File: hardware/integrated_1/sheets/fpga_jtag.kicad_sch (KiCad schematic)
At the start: 1 part, among them U1 XC6SLX9-TQG144

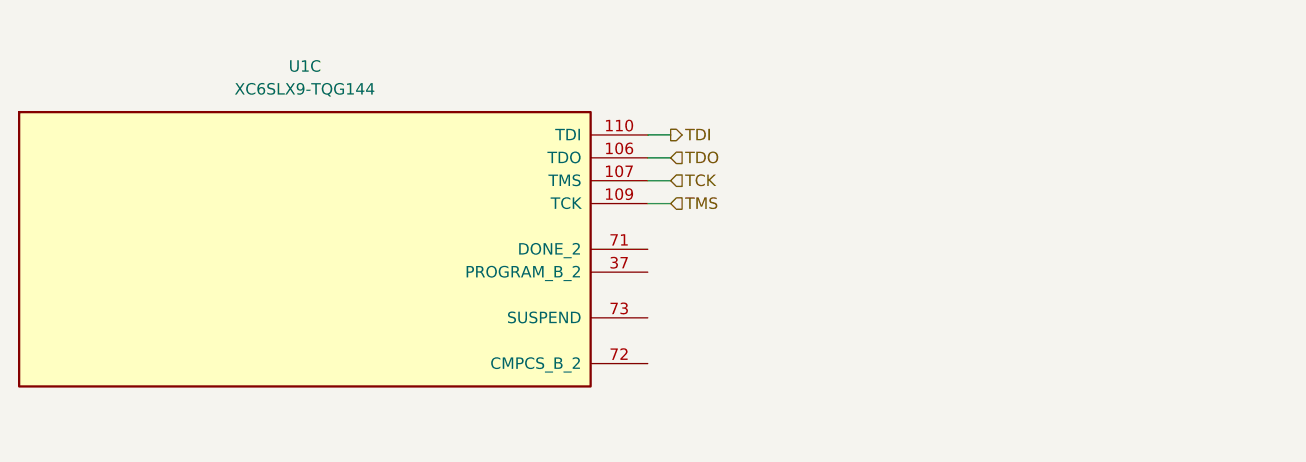
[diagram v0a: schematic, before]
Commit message: added async reset
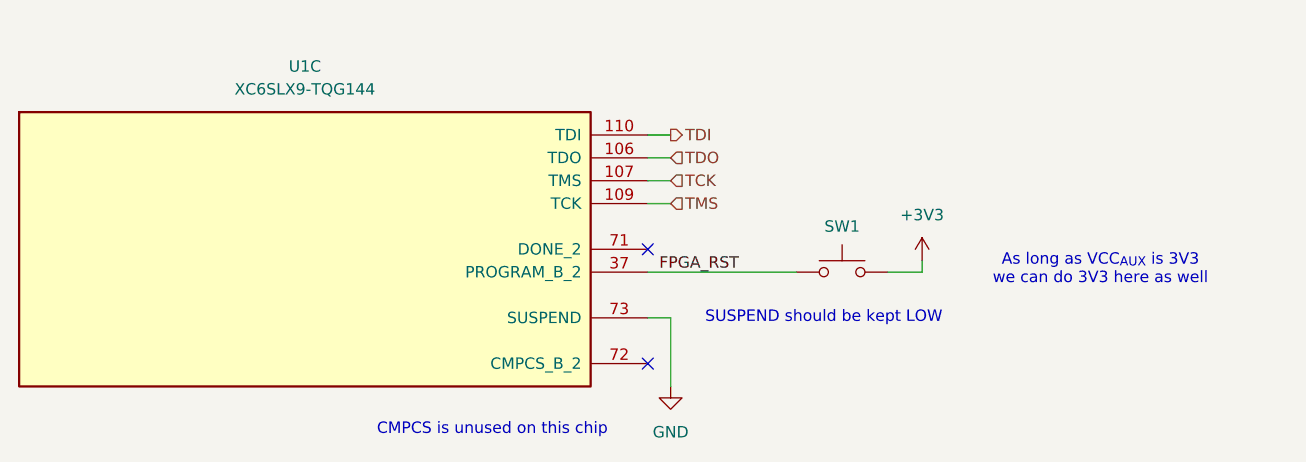
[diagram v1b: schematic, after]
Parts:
- added SW1: DNF, KiCAD Library:PTS636 SM25J SMTR LFS, symbol Switch:SW_Push
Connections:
- net FPGA_RST: now reaches U1.37 (PROGRAM_B_2)
- net FPGA_RST: now also SW1.1
- net GND: now reaches U1.73 (SUSPEND)
- new net +3V3: SW1.2
- no-connect marks 0 -> 2
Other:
- note added: "As long as VCC_{AUX} is 3V3 we can do 3V3 here as well"
- note added: "CMPCS is unused on this chip"
- note added: "SUSPEND should be kept LOW"

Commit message: finalizing the schematic and layout
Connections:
- net DONE: now reaches U1.71 (DONE_2)
- no-connect marks 2 -> 1
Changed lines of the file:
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@@
-	)
-	(no_connect
-		(at 173.99 87.63)
 	)
 	(no_connect
@@
 		)
 	)
+	(wire
+		(pts
+			(xy 176.53 87.63) (xy 173.99 87.63)
+		)
+		(stroke
+			(width 0)
+			(type default)
+		)
+	)
 	(text "SUSPEND should be kept LOW"
 		(exclude_from_sim no)
@@
 		(fields_autoplaced yes)
 		(effects
+			(font
+				(size 1.27 1.27)
+			)
+			(justify left)
+		)
+	)
+	(hierarchical_label "DONE"
+		(shape output)
+		(at 176.53 87.63 0)
+		(fields_autoplaced yes)
+		(effects

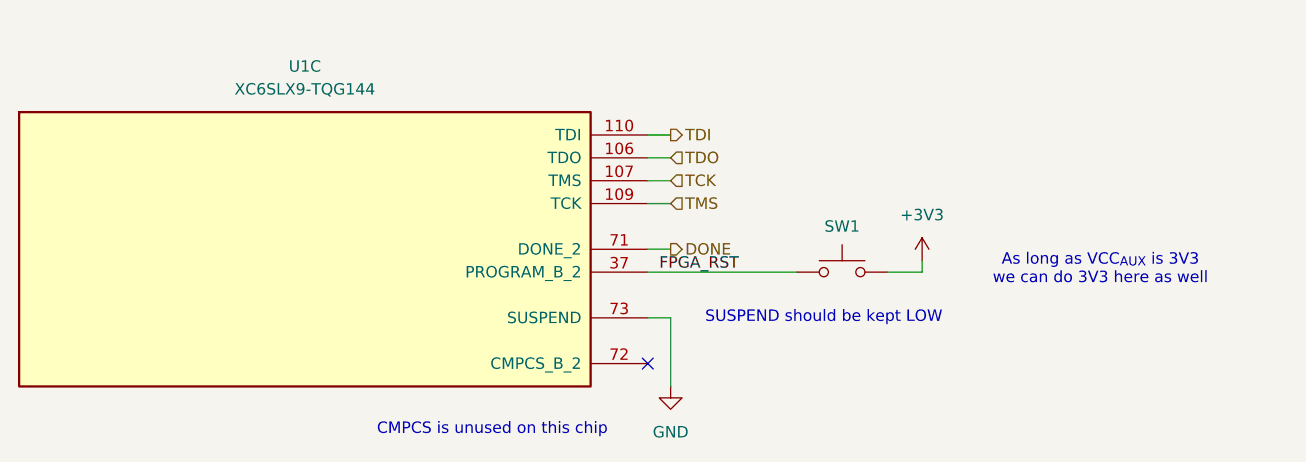
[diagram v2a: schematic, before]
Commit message: added testpoints
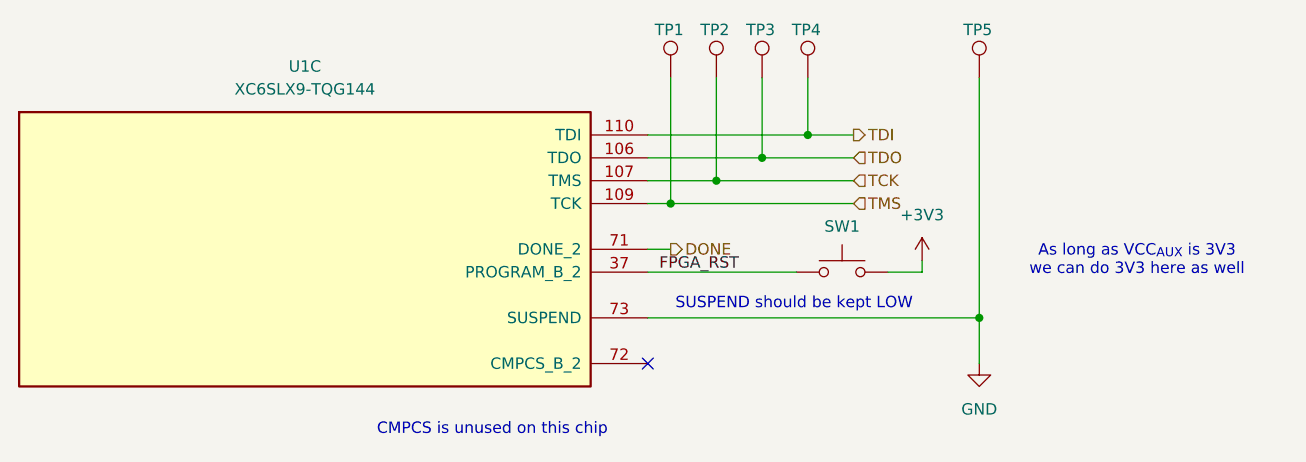
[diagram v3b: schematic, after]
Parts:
- added TP1, TP2, TP3, TP4, TP5: TestPoint, TestPoint:TestPoint_Pad_D1.0mm, symbol Connector:TestPoint
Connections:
- net GND: now also TP5.1
- net TCK: now also TP2.1
- net TDI: now also TP4.1
- net TDO: now also TP3.1
- net TMS: now also TP1.1
